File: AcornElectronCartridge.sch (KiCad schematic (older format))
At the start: 8 parts, among them P11 CONN_01X08, P12 CONN_01X08, P13 CONN_01X06, P21 CONN_01X06, P22 CONN_01X08, P23 CONN_01X08

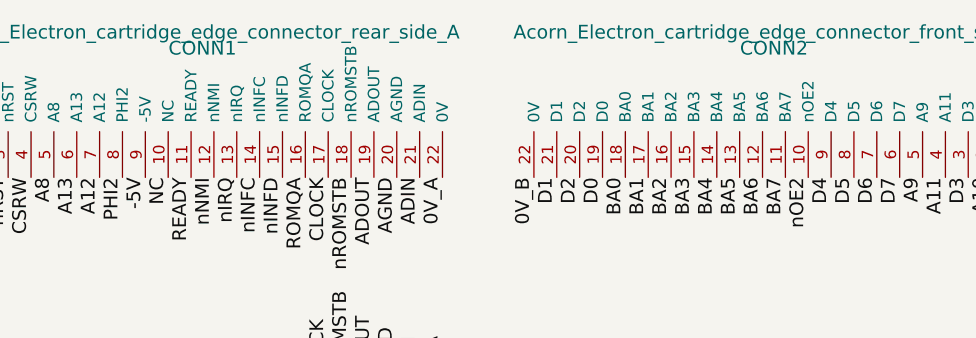
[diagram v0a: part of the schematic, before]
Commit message: Introduced separate front and rear edge connector footprints. Moved various labels on the edge connector components and footprints, also changing the visible name labels to use spaces instead of underscores.
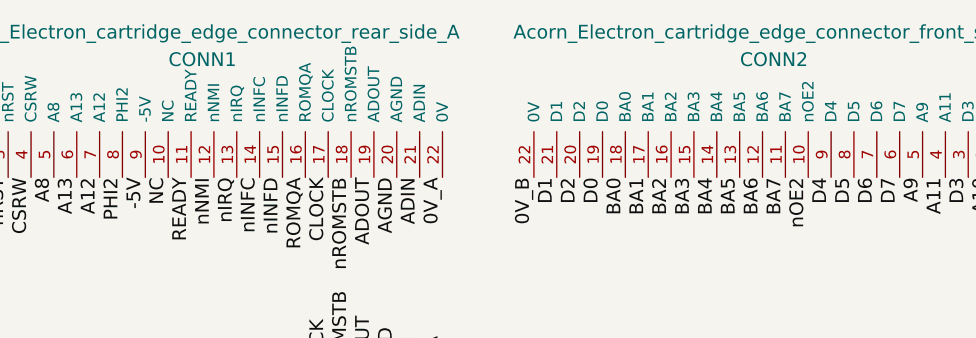
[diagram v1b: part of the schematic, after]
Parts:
- CONN1: footprint Acorn_Electron:Acorn_Electron_cartridge_edge_connector -> Acorn_Electron:Acorn_Electron_cartridge_edge_connector_rear
- CONN2: footprint Acorn_Electron:Acorn_Electron_cartridge_edge_connector -> Acorn_Electron:Acorn_Electron_cartridge_edge_connector_front
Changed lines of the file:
@@
 U 1 1 587CC811
 P 5250 1100
-F 0 "CONN2" H 5250 1100 60  0000 C TNN
+F 0 "CONN2" H 5250 1050 60  0000 C TNN
 F 1 "Acorn_Electron_cartridge_edge_connector_front_side_B" H 5250 1100 60  0000 C BNN
-F 2 "Acorn_Electron:Acorn_Electron_cartridge_edge_connector" H 5250 1100 60  0001 C CNN
+F 2 "Acorn_Electron:Acorn_Electron_cartridge_edge_connector_front" H 5250 1100 60  0001 C CNN
 F 3 "" H 5250 1100 60  0001 C CNN
 	1    5250 1100
@@
 U 1 1 587CC844
 P 2750 1100
-F 0 "CONN1" H 2750 1100 60  0000 C TNN
+F 0 "CONN1" H 2750 1050 60  0000 C TNN
 F 1 "Acorn_Electron_cartridge_edge_connector_rear_side_A" H 2750 1100 60  0000 C BNN
-F 2 "Acorn_Electron:Acorn_Electron_cartridge_edge_connector" H 2750 1100 60  0001 C CNN
+F 2 "Acorn_Electron:Acorn_Electron_cartridge_edge_connector_rear" H 2750 1100 60  0001 C CNN
 F 3 "" H 2750 1100 60  0001 C CNN
 	1    2750 1100
